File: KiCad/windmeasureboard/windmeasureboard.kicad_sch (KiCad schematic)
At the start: 3 parts, among them J1 ESQ-120-XX-X-D-XX, U1 TMS320F28379DPTPS

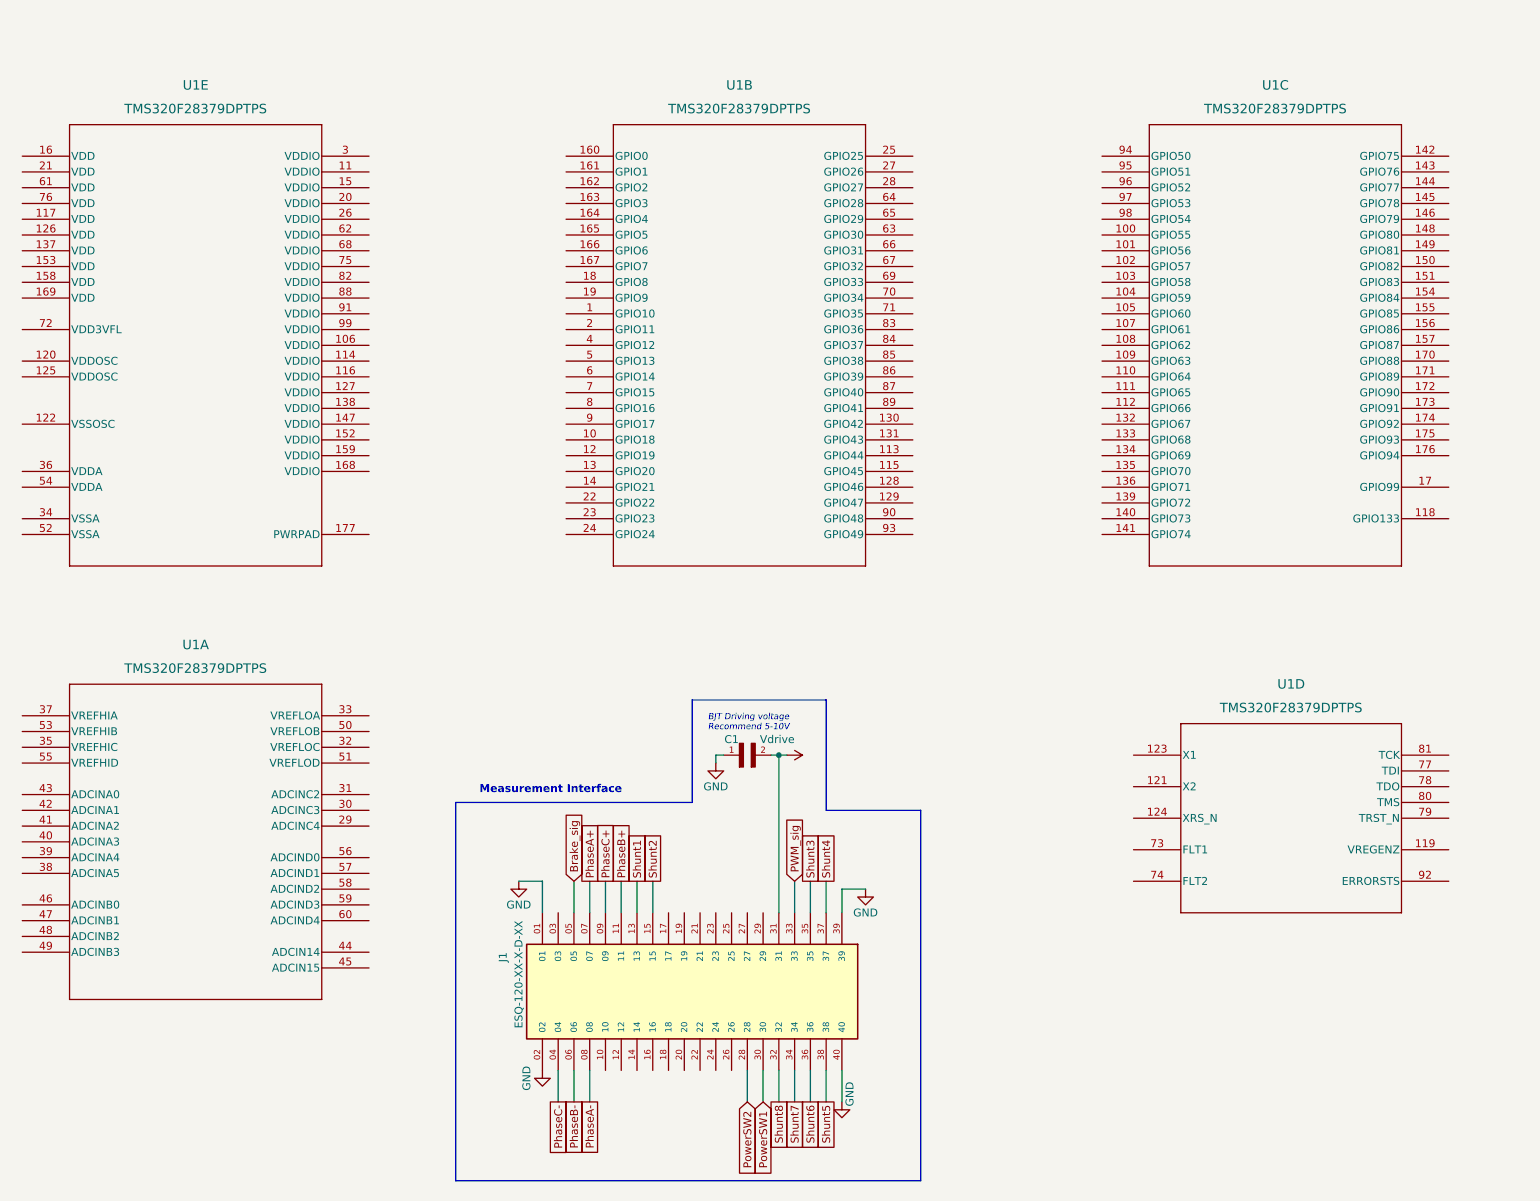
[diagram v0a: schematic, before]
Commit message: push before i swap out diodes for mosfets
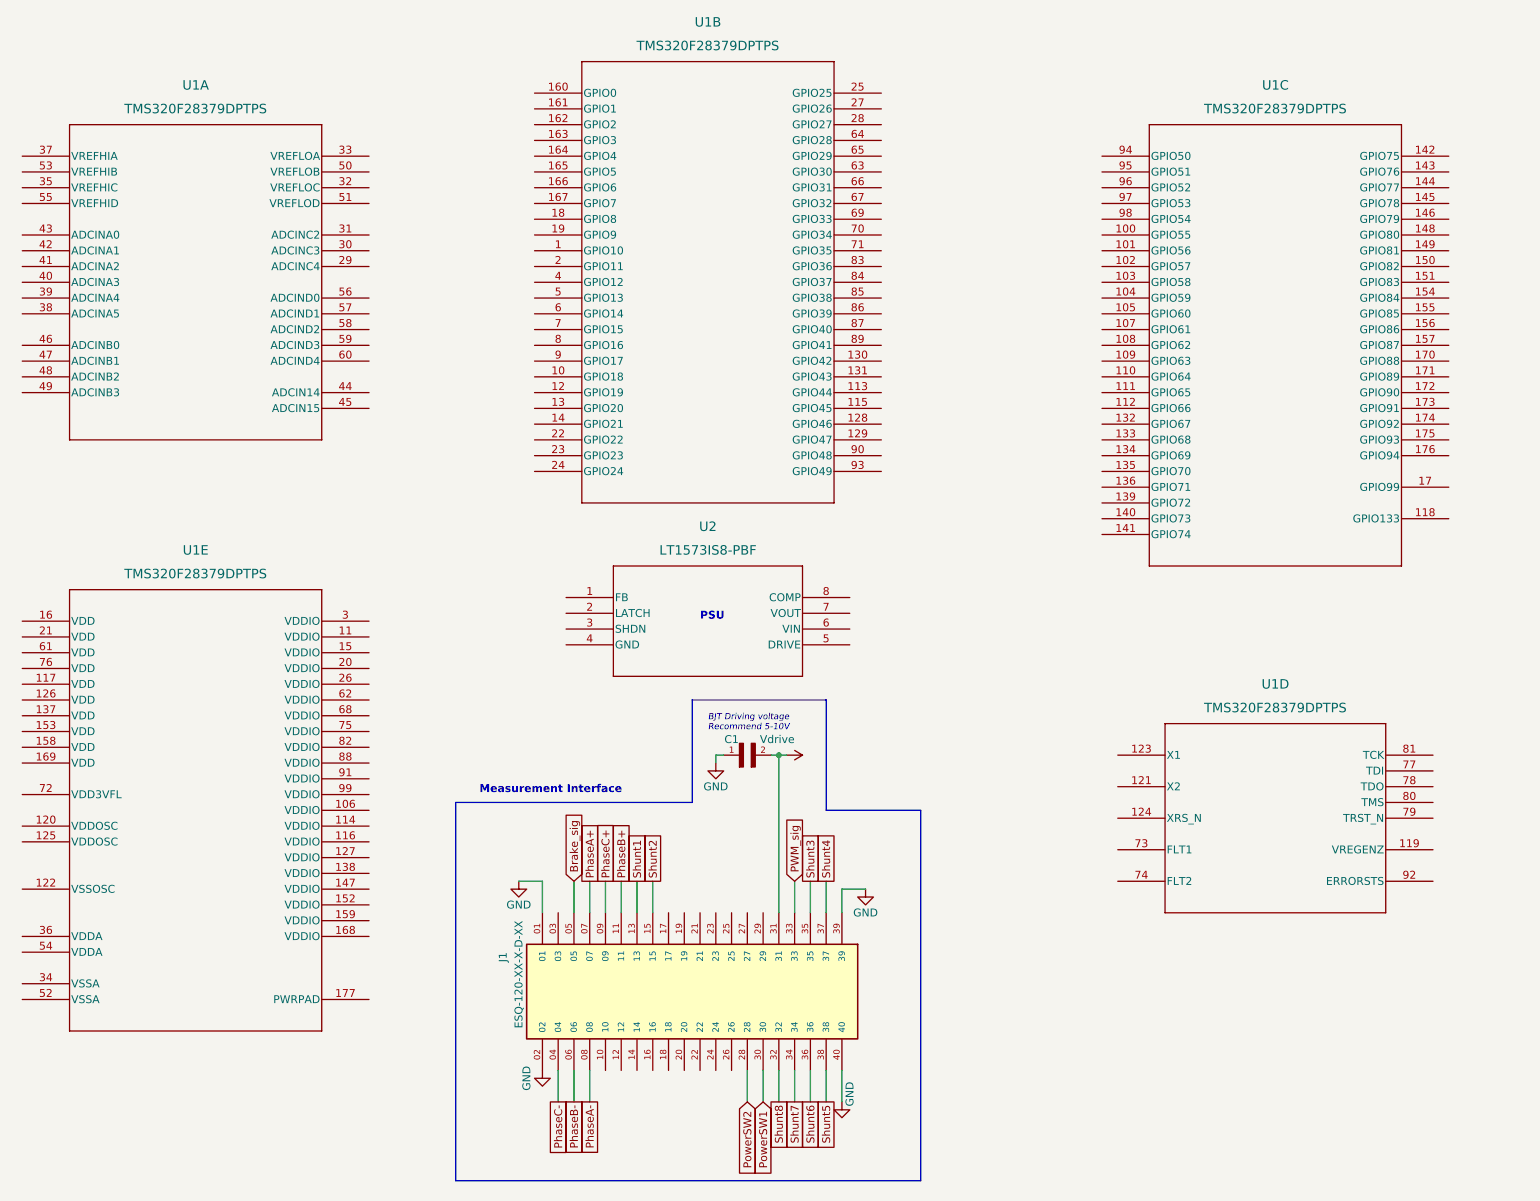
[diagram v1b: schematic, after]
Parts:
- added U2: LT1573IS8-PBF, footprints:SO-8_S_LIT, symbol LT1573IS8:LT1573IS8-PBF
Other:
- note added: "PSU"
- moved on the sheet: U1A, U1B, U1D, U1E
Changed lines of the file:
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@@
+    (effects (font (size 1.27 1.27) bold) (justify left bottom))
+  )
+  (text "PSU" (at 138.43 105.41 0)
     (effects (font (size 1.27 1.27) bold) (justify left bottom))
   )
@@
     )
   )
-  (symbol (lib_id "TMS320F28379DPTPS:TMS320F28379DPTPS") (at 144.78 60.96 0) (unit 2)
+  (symbol (lib_id "TMS320F28379DPTPS:TMS320F28379DPTPS") (at 139.7 50.8 0) (unit 2)
     (in_bom yes) (on_board yes) (fields_autoplaced)
-    (property "Reference" "U1" (id 0) (at 144.78 19.05 0)
+    (property "Reference" "U1" (id 0) (at 139.7 8.89 0)
       (effects (font (size 1.524 1.524)))
     )
-    (property "Value" "TMS320F28379DPTPS" (id 1) (at 144.78 22.86 0)
+    (property "Value" "TMS320F28379DPTPS" (id 1) (at 139.7 12.7 0)
       (effects (font (size 1.524 1.524)))
     )
-    (property "Footprint" "footprints:PTP0176F_N" (id 2) (at 144.78 60.96 0)
+    (property "Footprint" "footprints:PTP0176F_N" (id 2) (at 139.7 50.8 0)
       (effects (font (size 1.27 1.27) italic) hide)
     )
-    (property "Datasheet" "TMS320F28379DPTPS" (id 3) (at 144.78 60.96 0)
+    (property "Datasheet" "TMS320F28379DPTPS" (id 3) (at 139.7 50.8 0)
       (effects (font (size 1.27 1.27) italic) hide)
     )
@@
     (pin "1")
   )
-  (symbol (lib_id "TMS320F28379DPTPS:TMS320F28379DPTPS") (at 57.15 60.96 0) (unit 5)
+  (symbol (lib_id "TMS320F28379DPTPS:TMS320F28379DPTPS") (at 57.15 135.89 0) (unit 5)
     (in_bom yes) (on_board yes) (fields_autoplaced)
-    (property "Reference" "U1" (id 0) (at 57.15 19.05 0)
+    (property "Reference" "U1" (id 0) (at 57.15 93.98 0)
       (effects (font (size 1.524 1.524)))
     )
-    (property "Value" "TMS320F28379DPTPS" (id 1) (at 57.15 22.86 0)
+    (property "Value" "TMS320F28379DPTPS" (id 1) (at 57.15 97.79 0)
       (effects (font (size 1.524 1.524)))
     )
-    (property "Footprint" "footprints:PTP0176F_N" (id 2) (at 57.15 60.96 0)
+    (property "Footprint" "footprints:PTP0176F_N" (id 2) (at 57.15 135.89 0)
       (effects (font (size 1.27 1.27) italic) hide)
     )
-    (property "Datasheet" "TMS320F28379DPTPS" (id 3) (at 57.15 60.96 0)
+    (property "Datasheet" "TMS320F28379DPTPS" (id 3) (at 57.15 135.89 0)
       (effects (font (size 1.27 1.27) italic) hide)
     )
@@
     (pin "99")
   )
+  (symbol (lib_id "LT1573IS8:LT1573IS8-PBF") (at 116.84 101.6 0) (unit 1)
+    (in_bom yes) (on_board yes) (fields_autoplaced)
+    (property "Reference" "U2" (id 0) (at 139.7 90.17 0)
+      (effects (font (size 1.524 1.524)))
+    )
+    (property "Value" "LT1573IS8-PBF" (id 1) (at 139.7 93.98 0)
+      (effects (font (size 1.524 1.524)))
+    )
+    (property "Footprint" "footprints:SO-8_S_LIT" (id 2) (at 116.84 101.6 0)
+      (effects (font (size 1.27 1.27) italic) hide)
+    )
+    (property "Datasheet" "LT1573IS8-PBF" (id 3) (at 116.84 101.6 0)
+      (effects (font (size 1.27 1.27) italic) hide)
+    )
+    (pin "1")
+    (pin "2")
+    (pin "3")
+    (pin "4")
+    (pin "5")
+    (pin "6")
+    (pin "7")
+    (pin "8")
+  )
   (symbol (lib_id "power:Vdrive") (at 152.4 127 270) (unit 1)
     (in_bom yes) (on_board yes)
@@
     (pin "2")
   )
-  (symbol (lib_id "TMS320F28379DPTPS:TMS320F28379DPTPS") (at 57.15 140.97 0) (unit 1)
+  (symbol (lib_id "TMS320F28379DPTPS:TMS320F28379DPTPS") (at 57.15 50.8 0) (unit 1)
     (in_bom yes) (on_board yes) (fields_autoplaced)
-    (property "Reference" "U1" (id 0) (at 57.15 109.22 0)
+    (property "Reference" "U1" (id 0) (at 57.15 19.05 0)
       (effects (font (size 1.524 1.524)))
     )
-    (property "Value" "TMS320F28379DPTPS" (id 1) (at 57.15 113.03 0)
+    (property "Value" "TMS320F28379DPTPS" (id 1) (at 57.15 22.86 0)
       (effects (font (size 1.524 1.524)))
     )
-    (property "Footprint" "footprints:PTP0176F_N" (id 2) (at 57.15 140.97 0)
+    (property "Footprint" "footprints:PTP0176F_N" (id 2) (at 57.15 50.8 0)
       (effects (font (size 1.27 1.27) italic) hide)
     )
-    (property "Datasheet" "TMS320F28379DPTPS" (id 3) (at 57.15 140.97 0)
+    (property "Datasheet" "TMS320F28379DPTPS" (id 3) (at 57.15 50.8 0)
       (effects (font (size 1.27 1.27) italic) hide)
     )
@@
     (pin "99")
   )
-  (symbol (lib_id "TMS320F28379DPTPS:TMS320F28379DPTPS") (at 233.68 137.16 0) (unit 4)
+  (symbol (lib_id "TMS320F28379DPTPS:TMS320F28379DPTPS") (at 231.14 137.16 0) (unit 4)
     (in_bom yes) (on_board yes) (fields_autoplaced)
-    (property "Reference" "U1" (id 0) (at 233.68 115.57 0)
+    (property "Reference" "U1" (id 0) (at 231.14 115.57 0)
       (effects (font (size 1.524 1.524)))
     )
-    (property "Value" "TMS320F28379DPTPS" (id 1) (at 233.68 119.38 0)
+    (property "Value" "TMS320F28379DPTPS" (id 1) (at 231.14 119.38 0)
       (effects (font (size 1.524 1.524)))
     )
-    (property "Footprint" "footprints:PTP0176F_N" (id 2) (at 233.68 137.16 0)
+    (property "Footprint" "footprints:PTP0176F_N" (id 2) (at 231.14 137.16 0)
       (effects (font (size 1.27 1.27) italic) hide)
     )
-    (property "Datasheet" "TMS320F28379DPTPS" (id 3) (at 233.68 137.16 0)
+    (property "Datasheet" "TMS320F28379DPTPS" (id 3) (at 231.14 137.16 0)
       (effects (font (size 1.27 1.27) italic) hide)
     )
@@
       (reference "U1") (unit 5) (value "TMS320F28379DPTPS") (footprint "footprints:PTP0176F_N")
     )
-  )
+    (path "/38947d50-406f-4f28-9d57-65fc9601c729"
+      (reference "U2") (unit 1) (value "LT1573IS8-PBF") (footprint "footprints:SO-8_S_LIT")
+    )
+  )

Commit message: started work on Measure Board V1
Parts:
- removed C1: GRM32EC72A106KE05L, footprints:CAPC3225X270N, symbol GRM32EC72A106KE05L:GRM32EC72A106KE05L
- removed J1: ESQ-120-XX-X-D-XX, footprints:SAMTEC_ESQ-120-XX-X-D-XX, symbol ESQ-120-XX-X-D-XX:ESQ-120-XX-X-D-XX
- removed U1: TMS320F28379DPTPS, footprints:PTP0176F_N, symbol TMS320F28379DPTPS:TMS320F28379DPTPS
- removed U2: LT1573IS8-PBF, footprints:SO-8_S_LIT, symbol LT1573IS8:LT1573IS8-PBF
- added J?: ESQ-120-XX-X-D-XX, footprints:SAMTEC_ESQ-120-XX-X-D-XX, symbol ESQ-120-XX-X-D-XX:ESQ-120-XX-X-D-XX
- added U?: ESP32-S2-DEVKITC-1, ESP32-S2-DEVKITC-1:MODULE_ESP32-S2-DEVKITC-1, symbol ESP32-S2-DEVKITC-1:ESP32-S2-DEVKITC-1
- added U?: LM1084ISX-5.0_NOPB, TS3B, symbol LM1084ISX:LM1084ISX-5.0_NOPB
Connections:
- net GND: now also J?.01, J?.02, J?.39, U?.1 (ADJ/GND), U?.J1_22 (GND_J1_22), U?.J3_1 (GND_J3_1), U?.J3_21 (GND_J3_21), U?.J3_22 (GND_J3_22)
- net PWM_sig: now also J?.31
- net PhaseA+: now also J?.07
- net PhaseA-: now also J?.14
- net PhaseB+: now also J?.11
- net PhaseB-: now also J?.10
- net PhaseC+: now also J?.09
- net PhaseC-: now also J?.06
- net PowerSW1: now also J?.28
- net PowerSW2: now also J?.26
- net Shunt1: now also J?.25
- net Shunt2: now also J?.27
- net Shunt3: now also J?.33
- net Shunt4: now also J?.35
- net Shunt5: now also J?.36
- net Shunt6: now also J?.40, U?.3 (Vin), U?.4
- net Shunt7: now also J?.32
- net Shunt8: now also J?.30
- net Vdrive: now also J?.29
- new net Brake_Q1: J?.15
- new net Brake_Q2: J?.19
- new net Brake_Q3: J?.17
- new net Brake_Q4: J?.13
- new net Brake_Q5: J?.21
- new net Brake_Q6: J?.23
- new net Vsupp: U?.2 (Vout), U?.J1_21 (VCC_5V)
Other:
- note added: "Microcontroller"
- note added: "VBatt+"
- note added: "VDrive Voltage Recommend 5-10V"
- note removed: "BJT Driving voltage Recommend 5-10V"

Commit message: worked on measure board
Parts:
- added LED1, LED2, LED3, LED4, LED5, LED6: XZMG56W, LED_XZMG56W_SLD, symbol XZMG56W:XZMG56W
- U1: renamed from U?; footprint ESP32-S2-DEVKITC-1:MODULE_ESP32-S2-DEVKITC-1 -> footprints:MODULE_ESP32-S2-DEVKITC-1
- gave numbers to parts that had none: 2
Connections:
- net V3.3+: now reaches U1.J1_1 (3V3_J1_1)
- net V3.3+: now also LED1.2, LED2.2, LED3.2, LED4.2, LED5.2, LED6.2
- net LED6: now reaches U1.J1_2 (3V3_J1_2)
- net LED6: now also LED6.1
- net LED5: now reaches U1.J1_3 (EN)
- net LED5: now also LED5.1
- net LED4: now reaches U1.J1_4 (GPIO4)
- net LED4: now also LED4.1
- net LED3: now reaches U1.J1_5 (GPIO5)
- net LED3: now also LED3.1
- net LED2: now reaches U1.J1_6 (GPIO6)
- net LED2: now also LED2.1
- net LED1: now reaches U1.J1_7 (GPIO7)
- net LED1: now also LED1.1
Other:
- note added: "Indicators"
